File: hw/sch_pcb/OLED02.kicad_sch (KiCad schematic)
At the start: 23 parts, among them J2 HEADER_2x05_PARALLEL, M1 HOLE, M2 HOLE, M3 HOLE, M4 HOLE

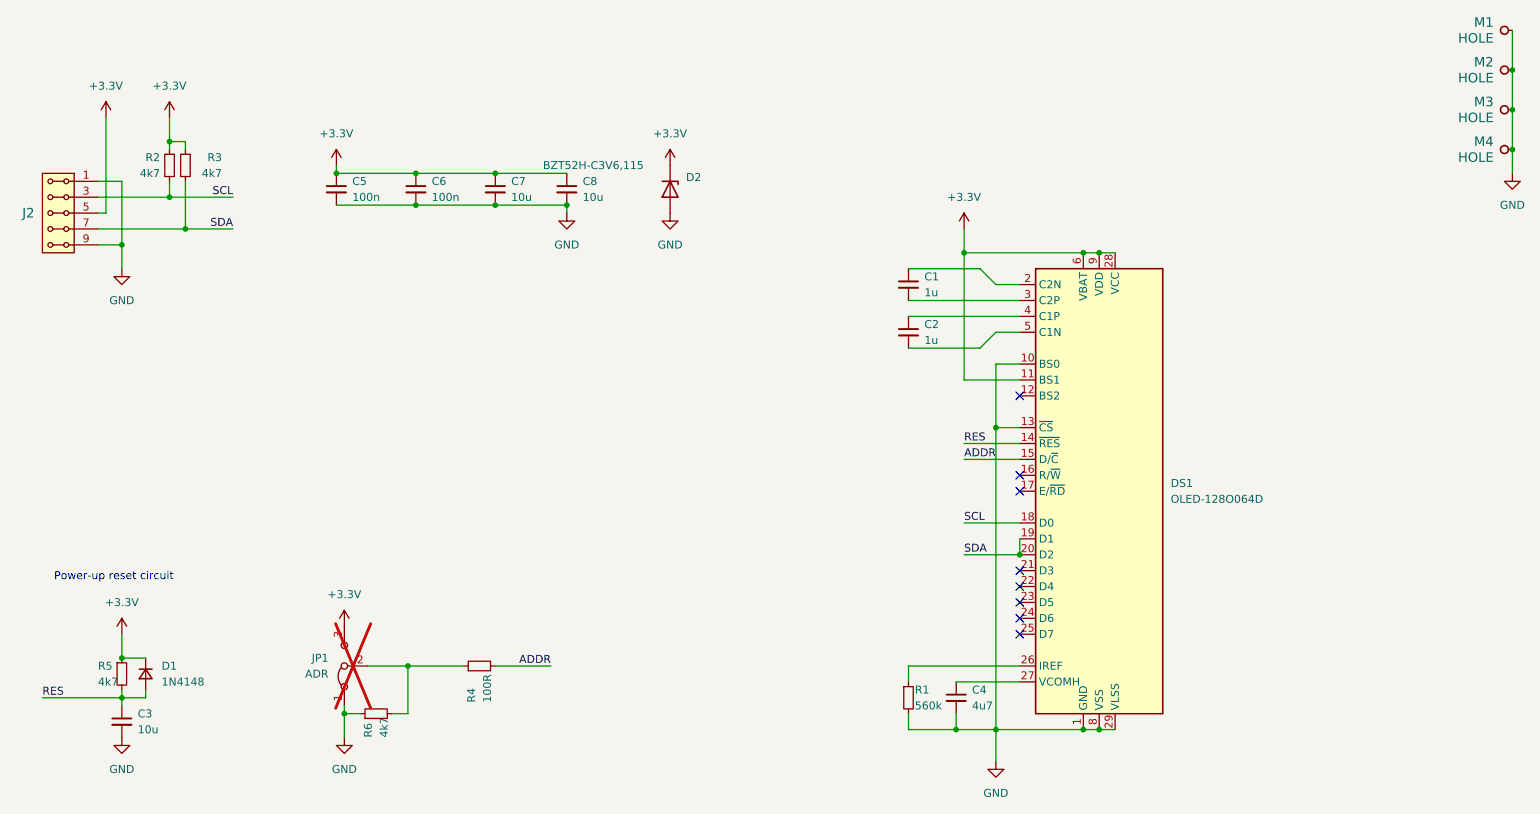
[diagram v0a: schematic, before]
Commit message: Update status and fab Layer.
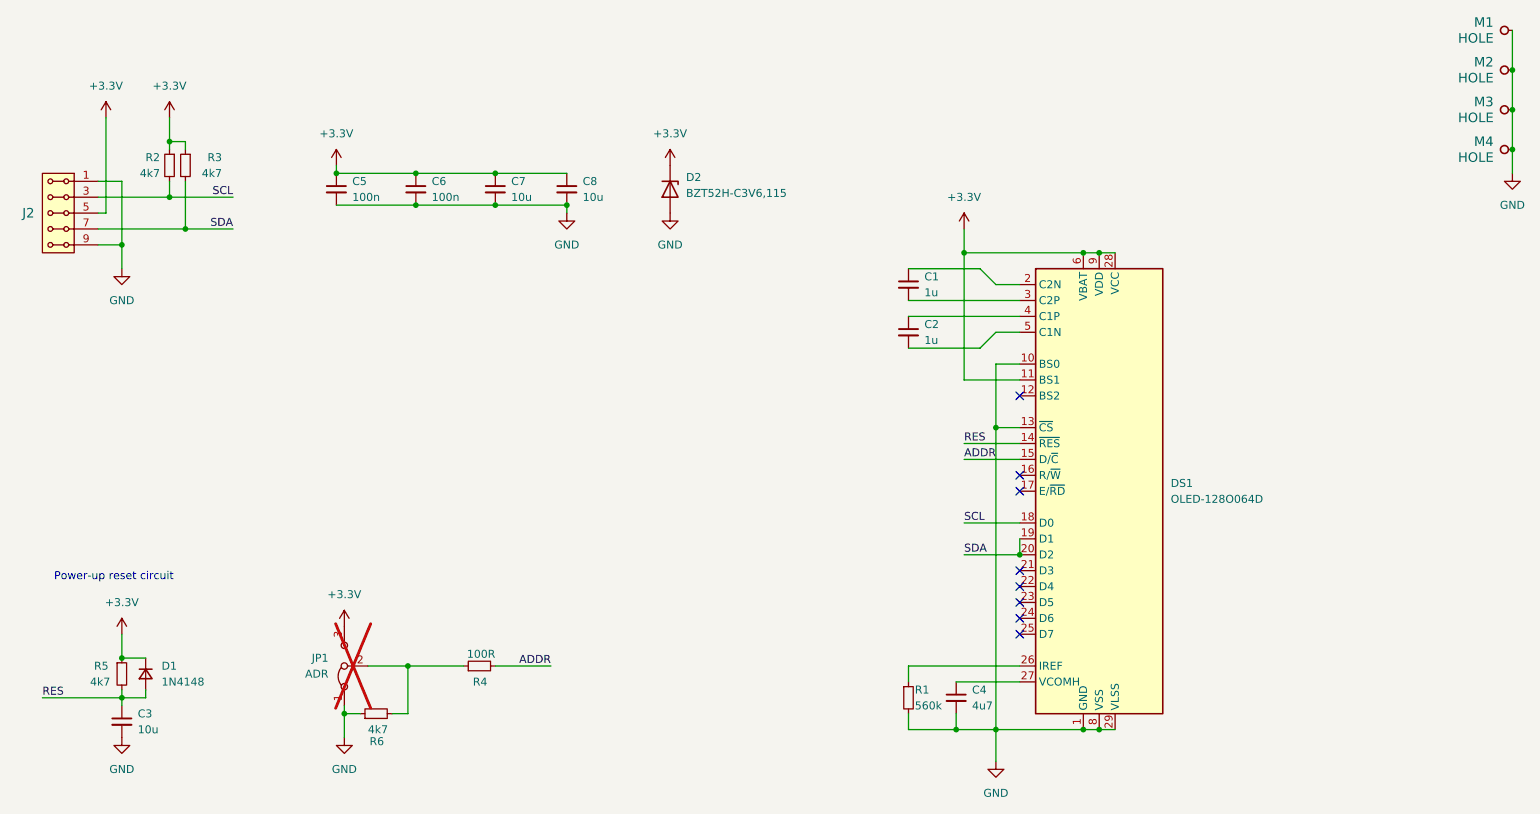
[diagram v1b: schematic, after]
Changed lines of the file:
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@@
 		(dnp no)
 		(property "Reference" "R4"
-			(at 104.14 129.032 0)
+			(at 106.68 125.73 90)
 			(effects
 				(font
@@
 		)
 		(property "Value" "100R"
-			(at 106.68 129.032 0)
+			(at 107.95 121.285 90)
 			(effects
 				(font
@@
 		)
 		(property "Value" "BZT52H-C3V6,115"
-			(at 115.57 43.18 90)
+			(at 138.43 47.625 90)
 			(effects
 				(font
@@
 		(dnp no)
 		(property "Reference" "R5"
-			(at 44.45 123.19 0)
+			(at 43.815 123.19 0)
 			(effects
 				(font
@@
 		)
 		(property "Value" "4k7"
-			(at 44.45 125.73 0)
+			(at 43.18 125.73 0)
 			(effects
 				(font
@@
 		(dnp no)
 		(property "Reference" "R6"
-			(at 87.63 134.62 0)
+			(at 90.17 135.255 90)
 			(effects
 				(font
@@
 		)
 		(property "Value" "4k7"
-			(at 90.17 134.62 0)
-			(effects
-				(font
+			(at 90.805 133.35 90)
+			(effects
+				(font

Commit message: update kicad version
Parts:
- added C9: 4u7, Capacitor_SMD:C_0805_2012Metric, symbol Device:C_Small
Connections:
- net +3.3V: no longer DS1.28 (VCC)
- net GND: now also DS1.12 (BS2), DS1.16 (R/~{W}), DS1.17 (E/~{RD}), DS1.21 (D3), DS1.22 (D4), DS1.23 (D5), DS1.24 (D6), DS1.25 (D7), C9.2
- new net: C9.1, DS1.28 (VCC)
- no-connect marks 8 -> 0
